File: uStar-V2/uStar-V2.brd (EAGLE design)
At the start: 88 x 88 mm, 48 parts, among them IC1 INA138, IC2 SN74HC4066PWRTSSOP, IC3 SN74HC4066PWRTSSOP, IC4 SN74HC4066PWRTSSOP, IC5 SN74HC4066PWRTSSOP, M1 Mount, M2 Mount, U2 SD_CARD, X2 BU-SMA-H, X3 BU-SMA-H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

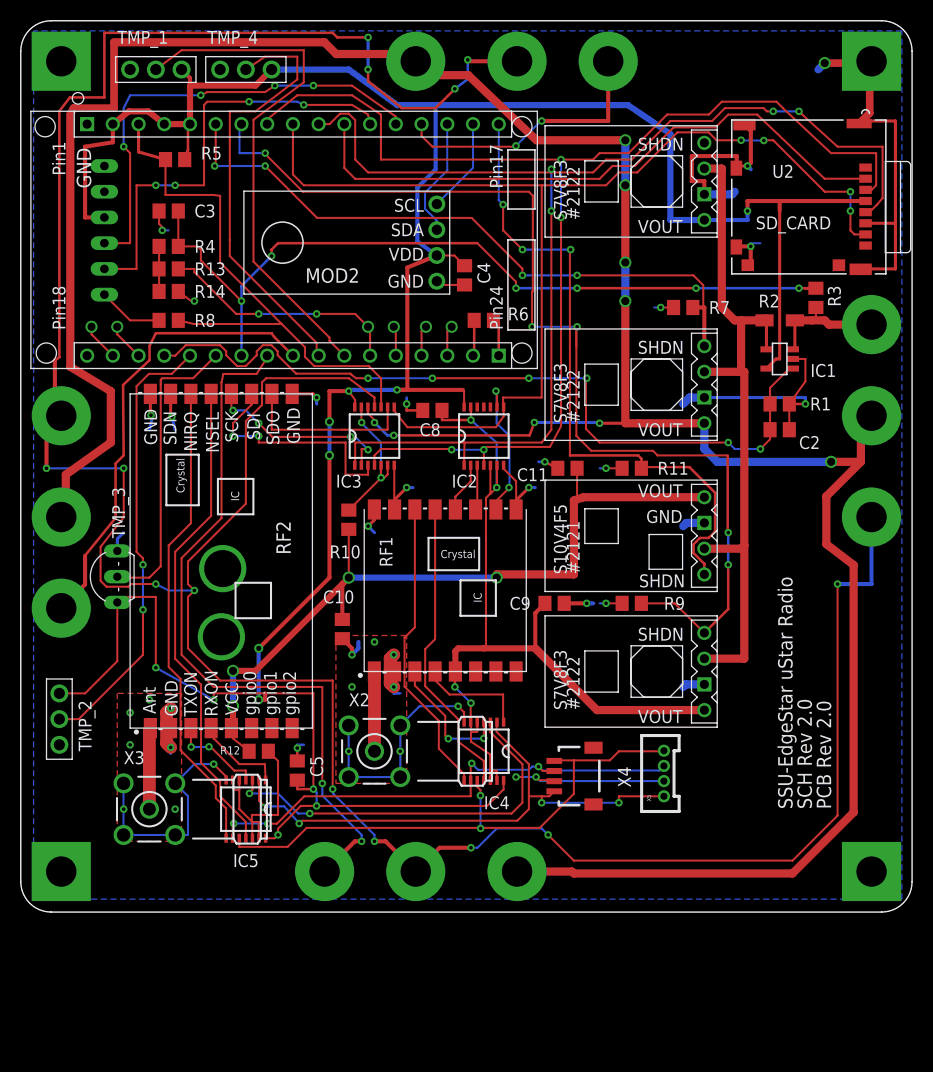
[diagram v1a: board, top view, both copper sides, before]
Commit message: 
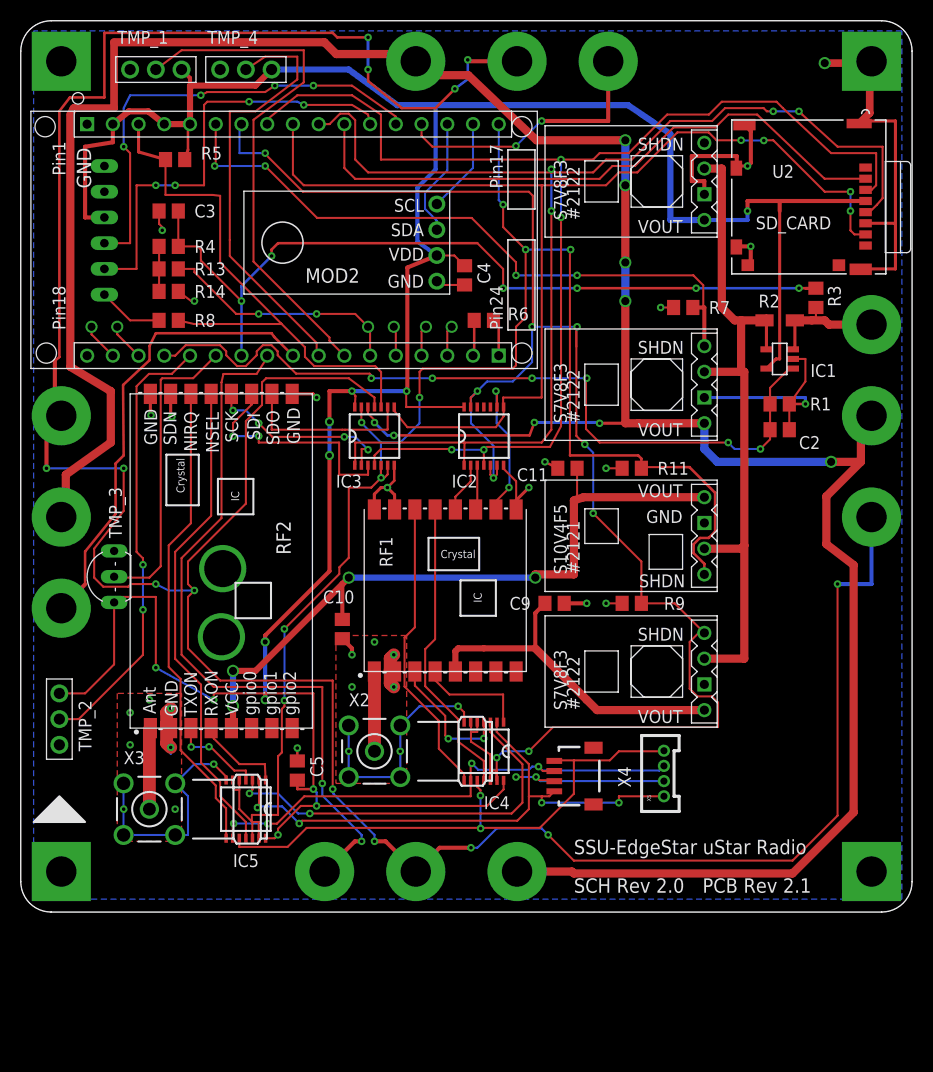
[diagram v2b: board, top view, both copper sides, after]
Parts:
- removed C8: 0.1uf, rcl:C0805
- removed R10, R12: 100K, rcl:R0805
- C2, C3: value 1uf -> 0.1uf
- moved TMP_3 0.32 mm to (9.22, 33.1)
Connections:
- net BOARD_VCC renamed BOARD_VCC_3.3
- net RAIL_SHDN renamed SYSTEM_RAIL_SHDN
- net SYSTEM_VCC renamed SYSTEM_VCC_3.3
- removed net N$4: IC3.13, IC3.5, IC3.6, R10.1
- removed net N$8: IC5.12, IC5.13, IC5.5, IC5.6, R12.2
- removed net RADIO_SHDN1: MOD1.P7, PWR3.SHDN, R9.2
- removed net RADIO_SHDN2: MOD1.P17, PWR4.SHDN, R11.2
- new net RADIO1_SHDN: IC2.13, IC2.5, IC2.6, IC4.12, IC4.13, IC4.5, IC4.6, MOD1.P7, PWR3.SHDN, R9.2
- new net RADIO2_SHDN: IC3.13, IC3.5, IC3.6, IC5.12, IC5.13, IC5.5, IC5.6, MOD1.P17, PWR4.SHDN, R11.2
- net GND: no longer C8.2
- net RADIO_VCC_3_3: no longer C8.1, IC2.13, IC2.5, IC2.6, IC4.12, IC4.13, IC4.5, IC4.6
- net RADIO_VCC_5V: no longer R10.2, R12.1
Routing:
- net RADIO1_SHDN: track 0.00 -> 160.6 mm, vias 0 -> 9
- net RADIO2_SHDN: track 0.00 -> 158.9 mm, vias 0 -> 8
- net RADIO_SHDN1: track 103.6 -> 0.00 mm, vias 5 -> 0
- net RADIO_SHDN2: track 64.9 -> 0.00 mm, vias 3 -> 0
- net RADIO_VCC_3_3: track 84.5 -> 34.6 mm, vias 4 -> 0
- net GND: track 212.4 -> 179.2 mm, vias 34 -> 32
- net N$8: track 20.1 -> 0.00 mm
- net N$4: track 15.3 -> 0.00 mm, vias 2 -> 0
- net RADIO_VCC_5V: track 78.4 -> 70.5 mm
- net BOARD_VCC_3.3: track 297.5 -> 295.6 mm
- net V_BATT: track 81.8 -> 82.5 mm
- net 1WIRE_BUS: track 287.0 -> 287.6 mm
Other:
- board text added: "PCB Rev 2.1"

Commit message: Changed solder stop mask to fully cover vias to protect from short with RFM23bp. Changed brd rev label to 2.1b to reflect above. Added R9 and R11 back into the flight build - Inadvertently removed when adding the GND station build option. Added wiring schematic for FTDI cable and connector to sch Added ECO sheet to sch change or R6 to Capacitor 0.1uf -- Reset Issue resolve.
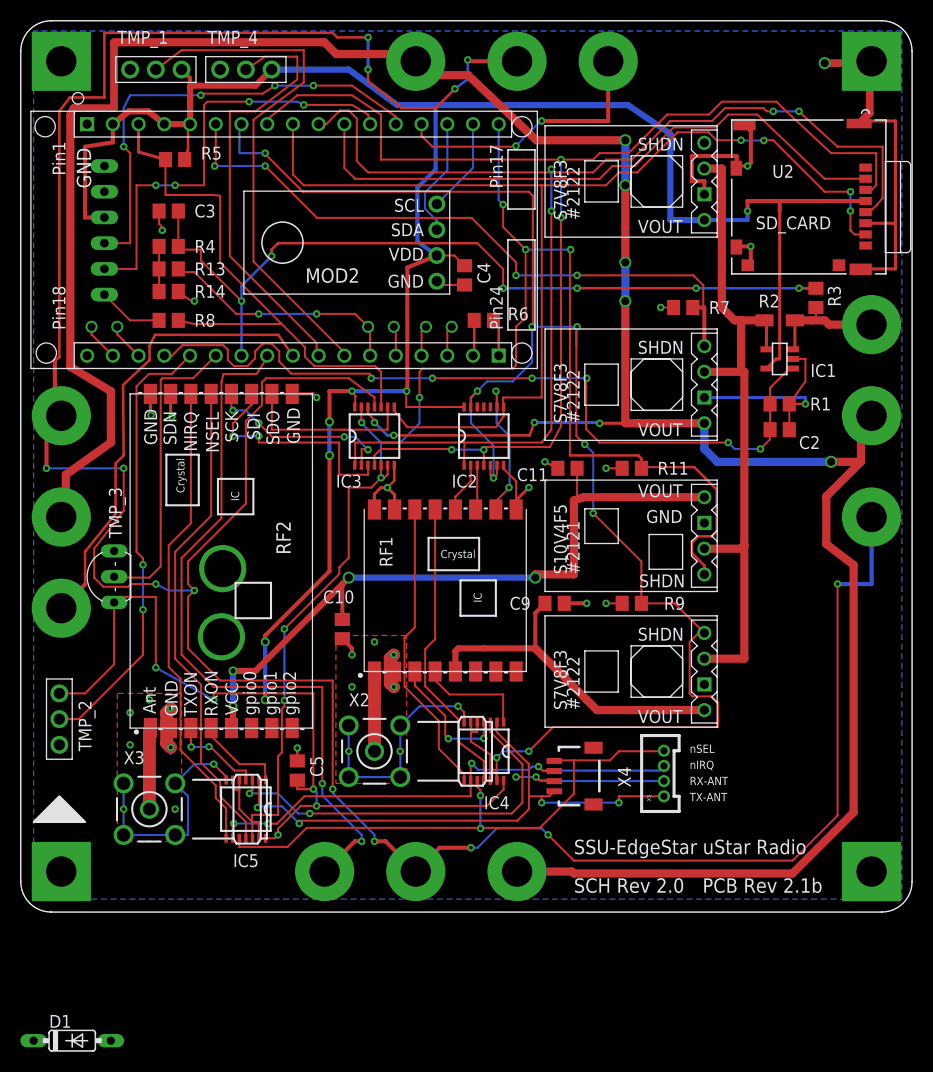
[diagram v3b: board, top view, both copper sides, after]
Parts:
- added D1: 1N4148DO35-7, diode:DO35-7
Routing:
- net I_BVATTERY: track 78.6 -> 79.7 mm
- net RADIO2_SHDN: track 158.9 -> 159.7 mm
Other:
- board text added: "PCB Rev 2.1b"
- board text added: "RX-ANT"
- board text added: "TX-ANT"
- board text added: "nIRQ"
- board text added: "nSEL"
- board text removed: "PCB Rev 2.1"
